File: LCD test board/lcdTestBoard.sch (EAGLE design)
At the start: 1 part

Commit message: Update lcdTestBoard.sch
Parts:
- added C1, C4: 7p, rcl:C-EUC0603
- added C2, C5: 2,2u, rcl:C-EUC0603
- added C3, C6: (no value), rcl:C-EUC0603
- added R1, R4: 1k, rcl:R-EU_R0603
- added R2, R5: (no value), rcl:R-EU_R0603
- added R3, R6: 51,1k, rcl:R-EU_R0603
- added SV1, SV2: (no value), con-lstb:MA04-2
- added SV3: (no value), con-lstb:MA03-1
- added U$1, U$6: LP2980-ADJ, LP2980:LP2980-ADJ
- added U$3: MCP1662, MCP1662:MCP1662
- added U$4: TPS62260, TPS6226x:TPS62260
- added U$5: ST2378E_TSSOP, ST2378E:ST2378E_TSSOP
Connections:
- new net 1.8: SV1.6, SV1.8
- new net 1.8V_LDO: C1.2, C2.1, R2.1, U$1.VOUT
- new net 1.8_LDO: SV1.7
- new net 1.8_STEP: SV1.5
- new net 2.8: SV1.2, SV1.4
- new net 2.8V_LDO: C4.2, C5.1, R5.1, U$6.VOUT
- new net 2.8_LDO: SV1.3
- new net 2.8_STEP: SV1.1
- new net 3V_R: CON1_P2.3V@5, CON1_P2.3V@6, SV2.7
- new net 5V_R: CON1_P2.5V@3, CON1_P2.5V@4, SV2.5
- new net GND: C2.2, C3.1, C5.2, C6.1, CON1_P1.GND@1, CON1_P1.GND@2, CON1_P1.GND@23, CON1_P1.GND@49, CON1_P1.GND@5, CON1_P1.GND@50, CON1_P2.GND@1, CON1_P2.GND@2, CON1_P2.GND@49, CON1_P2.GND@50, R3.1, R6.1, SV2.1, SV3.3, U$1.GND, U$6.GND
- new net N$1: R1.1, U$1.ON/OFF(N)
- new net N$3: C1.1, R2.2, R3.2, U$1.ADJ
- new net N$6: R4.1, U$6.ON/OFF(N)
- new net N$7: SV2.3, SV3.1
- new net N$8: C4.1, R5.2, R6.2, U$6.ADJ
- new net V: C3.2, C6.2, R1.2, R4.2, SV2.2, SV2.4, SV2.6, SV2.8, U$1.VIN, U$6.VIN
- new net VDD: CON1_P1.VDD@3, CON1_P1.VDD@4
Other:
- note added: "1.8V LDO"
- note added: "1.8V LDO 1.8V STEP DOWN 2.8V LDO 2.8V STEP DOWN"
- note added: "2.8V LDO"
- note added: "DISC 3V DISC 5V OUT 3V OUT 5V"
- note added: "Volteage soure select"
- note added: "Voltyge main selector"
- moved on the sheet: CON1_P1, CON1_P2

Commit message: Update lcdTestBoard.sch
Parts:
- added C10, C7: 4.7u, rcl:C-EUC0603
- added C11, C8: 22p, rcl:C-EUC0603
- added C12, C13, C14, C9: 10u, rcl:C-EUC0603
- added D1: BAS40, diode:BAS40
- added L1, L2, L3: 2.2u, rcl:L-USL2012C
- added R10, R7: 180k, rcl:R-EU_R0603
- added R11: 10R, rcl:R-EU_R0603
- added R8: 360k, rcl:R-EU_R0603
- added R9: 680k, rcl:R-EU_R0603
- added SV4: (no value), con-lstb:MA03-1
- added U$2: ST2378E_TSSOP, ST2378E:ST2378E_TSSOP
- added U$7: TPS62260, TPS6226x:TPS62260
- C3, C6: value (none) -> 1u
- R2: value (none) -> 23.7k
- R5: value (none) -> 64.9k
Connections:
- removed net VDD: CON1_P1.VDD@3, CON1_P1.VDD@4
- new net N$10: C8.2, R7.2, R8.1, U$4.FB
- new net N$12: SV4.2, U$3.EN
- new net N$13: D1.A, L3.2, U$3.SW
- new net N$2: L2.1, U$7.SW
- new net N$4: C11.2, R10.2, R9.1, U$7.FB
- new net N$5: L1.1, U$4.SW
- new net V_LCD_N: R11.1, U$3.VFB
- new net V_LCD_P: C13.1, D1.C
- net 1.8_STEP: now also C8.1, C9.1, L1.2, R8.2
- net 2.8_STEP: now also C11.1, C12.1, L2.2, R9.2
- net GND: now also C10.2, C12.2, C13.2, C14.2, C7.2, C9.2, R10.1, R11.2, R7.1, U$3.GND, U$4.GND, U$7.GND
- net V: now also C10.1, C14.1, C7.1, L3.1, SV4.1, U$3.VIN, U$4.EN, U$4.VIN, U$7.EN, U$7.VIN
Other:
- note added: "1.8V STEP DOWN"
- note added: "2.8V STEP DOWN"
- note added: "Curent selector resistor"
- note added: "LCD power regulator"
- note added: "always on external on/off"
- moved on the sheet: U$3, U$4, U$5

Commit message: Update lcdTestBoard.sch
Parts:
- added R12, R13: 1k, rcl:R-EU_R0603
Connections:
- net 1.8 renamed 1.8V
- net 2.8 renamed 2.8V
- net N$1 renamed 1.8_LDO_EN
- net N$6 renamed 2.8_LDO_EN
- new net 1.8_STEP_EN: R12.2, U$4.EN
- new net 2.8_STEP_EN: R13.2, U$7.EN
- new net LCD_POWER_EN: SV4.3
- net GND: now also R1.2, R12.1, R13.1, R4.2
- net V: no longer R1.2, R4.2, U$4.EN, U$7.EN
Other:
- note added: "do rozdzielenia"
- moved on the sheet: C3, C6, L3, R11

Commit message: Update lcdTestBoard.sch
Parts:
- removed SV1: (no value), con-lstb:MA04-2
- added C15: 7p, rcl:C-EUC0603
- added C16: 2,2u, rcl:C-EUC0603
- added C17: 1u, rcl:C-EUC0603
- added C18: 4.7u, rcl:C-EUC0603
- added C19: 22p, rcl:C-EUC0603
- added C20: 10u, rcl:C-EUC0603
- added L4: 2.2u, rcl:L-USL2012C
- added R14, R19: 1k, rcl:R-EU_R0603
- added R15: 82k, rcl:R-EU_R0603
- added R16: 51,1k, rcl:R-EU_R0603
- added R17: 820k, rcl:R-EU_R0603
- added R18: 180k, rcl:R-EU_R0603
- added R20: 3,9k, rcl:R-EU_R0603
- added SV5: (no value), con-lstb:MA06-2
- added U$8: LP2980-ADJ, LP2980:LP2980-ADJ
- added U$9: TPS62260, TPS6226x:TPS62260
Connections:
- new net 3.3V: SV5.2, SV5.4
- new net 3.3V_LDO: C15.2, C16.1, R20.2, U$8.VOUT
- new net 3.3_LDO: SV5.3
- new net 3.3_LDO_EN: R14.1, U$8.ON/OFF(N)
- new net 3.3_STEP: C19.1, C20.1, L4.2, R17.2, SV5.1
- new net 3.3_STEP_EN: R19.2, U$9.EN
- new net N$1: C15.1, R15.2, R16.2, U$8.ADJ
- new net N$11: R15.1, R20.1
- new net N$6: L4.1, U$9.SW
- new net N$9: C19.2, R17.1, R18.2, U$9.FB
- net 1.8V: now also SV5.10, SV5.12; no longer SV1.6, SV1.8
- net 1.8_LDO: now also SV5.11; no longer SV1.7
- net 1.8_STEP: now also SV5.9; no longer SV1.5
- net 2.8V: now also SV5.6, SV5.8; no longer SV1.2, SV1.4
- net 2.8_LDO: now also SV5.7; no longer SV1.3
- net 2.8_STEP: now also SV5.5; no longer SV1.1
- net GND: now also C16.2, C17.1, C18.2, C20.2, R14.2, R16.1, R18.1, R19.1, U$8.GND, U$9.GND
- net V: now also C17.2, C18.1, U$8.VIN, U$9.VIN
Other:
- note added: "1.8V LDO 1.8V STEP DOWN 2.8V LDO 2.8V STEP DOWN 3.3V LDO 3.3V STEP DOWN"
- note added: "3.3V LDO"
- note added: "3.3V STEP DOWN"
- note added: "DISC 3V DISC 5V IN 3.3V IN 5V"
- note removed: "1.8V LDO 1.8V STEP DOWN 2.8V LDO 2.8V STEP DOWN"
- note removed: "DISC 3V DISC 5V OUT 3V OUT 5V"
- moved on the sheet: C1, C10, C11, C12, C13, C14, C2, C3, C4, C5, C6, C7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

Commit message: Update lcdTestBoard.sch
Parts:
- removed U$2, U$5: ST2378E_TSSOP, ST2378E:ST2378E_TSSOP
- added CON2: AXE534124, con_AXE534124:AXE534124
- added SV1: (no value), con-lstb:MA04-2
- added U2, U5: ST2378E_TSSOP, ST2378E:ST2378E_TSSOP
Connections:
- new net LCD_BL_PWM: CON2.LCD_BL_PWM
- new net LCD_CS: CON2.CS
- new net LCD_D0: CON2.D0
- new net LCD_D1: CON2.D1
- new net LCD_D10: CON2.D10
- new net LCD_D11: CON2.D11
- new net LCD_D12: CON2.D12
- new net LCD_D13: CON2.D13
- new net LCD_D14: CON2.D14
- new net LCD_D15: CON2.D15
- new net LCD_D2: CON2.D2
- new net LCD_D3: CON2.D3
- new net LCD_D4: CON2.D4
- new net LCD_D5: CON2.D5
- new net LCD_D6: CON2.D6
- new net LCD_D7: CON2.D7
- new net LCD_D8: CON2.D8
- new net LCD_D9: CON2.D9
- new net LCD_RE: CON2.RE
- new net LCD_RES: CON2.RES
- new net LCD_RS: CON2.RS
- new net LCD_TE: CON2.TE
- new net LCD_WE: CON2.WE
- net 1.8V: now also CON2.VO_DIG, SV1.7, SV1.8
- net 2.8V: now also CON2.VO_LCD_2.8, SV1.5, SV1.6
- net 3.3V: now also SV1.3, SV1.4
- net GND: now also CON2.GND, CON2.Z1, CON2.Z2, CON2.Z3, CON2.Z4, SV1.1, SV1.2
- net V_LCD_N: now also CON2.LCD_BL_K
- net V_LCD_P: now also CON2.LCD_BL_A
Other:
- note added: "Discovery conector"
- note added: "Sony Ericsson U5 Vivaz display"
- note added: "Voltage output"
- moved on the sheet: CON1_P1, CON1_P2

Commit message: Update lcdTestBoard.sch
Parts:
- added U$2: PJST19GL50, con_jack_2.5:PJST19GL50
- added U1: LP2980-ADJ, LP2980:LP2980-ADJ
- added U3: MCP1662, MCP1662:MCP1662
- added U4: TPS62260, TPS6226x:TPS62260
- U$1: value LP2980-ADJ -> PJST19GL50; device LP2980:LP2980-ADJ -> con_jack_2.5:PJST19GL50
- U$3: value MCP1662 -> PJST2538GSD; device MCP1662:MCP1662 -> con_jack_2.5:PJST2538GSD
- U$4: value TPS62260 -> PJST2538GSD; device TPS6226x:TPS62260 -> con_jack_2.5:PJST2538GSD
- renumbered U$6 to U6, U$7 to U7, U$8 to U8, U$9 to U9
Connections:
- net 1.8V_LDO: now also U1.VOUT; no longer U$1.VOUT
- net 1.8_LDO_EN: now also U1.ON/OFF(N); no longer U$1.ON/OFF(N)
- net 1.8_STEP_EN: now also U4.EN; no longer U$4.EN
- net GND: now also U1.GND, U3.GND, U4.GND; no longer U$1.GND, U$3.GND, U$4.GND
- net N$10: now also U4.FB; no longer U$4.FB
- net N$12: now also U3.EN; no longer U$3.EN
- net N$13: now also U3.SW; no longer U$3.SW
- net N$3: now also U1.ADJ; no longer U$1.ADJ
- net N$5: now also U4.SW; no longer U$4.SW
- net V: now also U1.VIN, U3.VIN, U4.VIN; no longer U$1.VIN, U$3.VIN, U$4.VIN
- net V_LCD_N: now also U3.VFB; no longer U$3.VFB

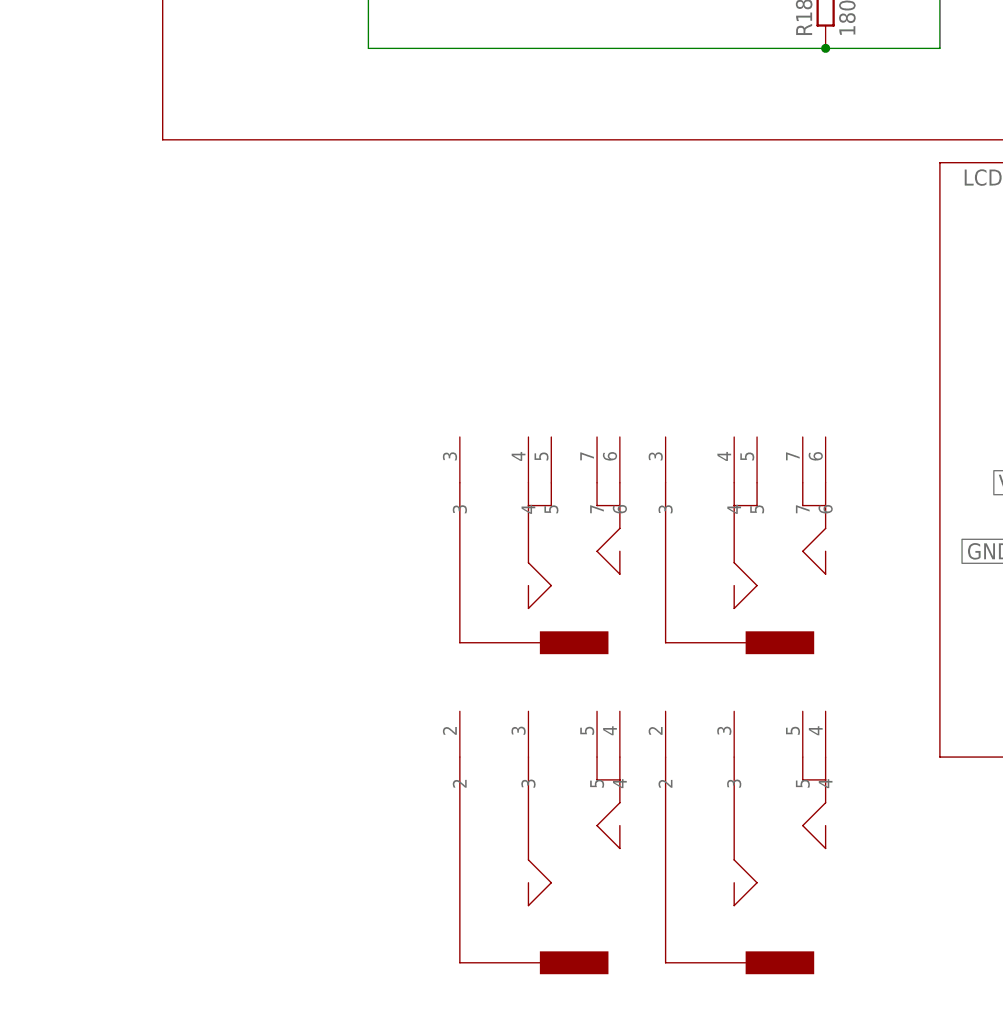
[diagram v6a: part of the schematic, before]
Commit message: dodano zlacza do stackmaty i wyswietlacza
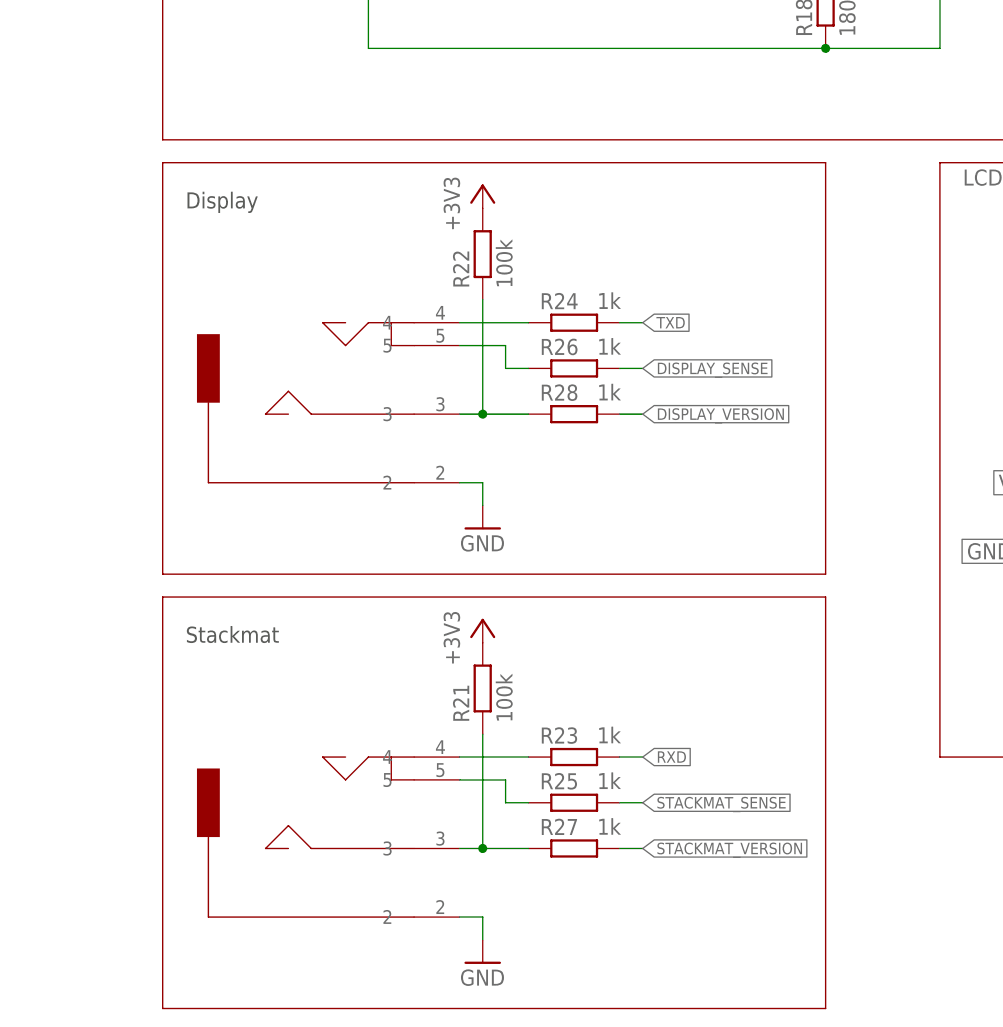
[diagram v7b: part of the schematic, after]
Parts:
- removed U$3, U$4: PJST2538GSD, con_jack_2.5:PJST2538GSD
- added R21, R22: 100k, rcl:R-EU_R0603
- added R23, R24, R25, R26, R27, R28: 1k, rcl:R-EU_R0603
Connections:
- new net +3V3: R21.2, R22.2
- new net DISPLAY_SENSE: R26.1
- new net DISPLAY_VERSION: R28.1
- new net N$14: R22.1, R28.2, U$2.3
- new net N$15: R21.1, R27.2, U$1.3
- new net N$16: R24.2, U$2.4
- new net N$17: R23.2, U$1.4
- new net N$18: R26.2, U$2.5
- new net N$19: R25.2, U$1.5
- new net RXD: R23.1
- new net STACKMAT_SENSE: R25.1
- new net STACKMAT_VERSION: R27.1
- new net TXD: R24.1
- net GND: now also U$1.2, U$2.2
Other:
- note added: "Display"
- note added: "Stackmat"
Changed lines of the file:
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@@
 <part name="U$1" library="con_jack_2.5" deviceset="PJST19GL50" device=""/>
 <part name="U$2" library="con_jack_2.5" deviceset="PJST19GL50" device=""/>
-<part name="U$3" library="con_jack_2.5" deviceset="PJST2538GSD" device=""/>
-<part name="U$4" library="con_jack_2.5" deviceset="PJST2538GSD" device=""/>
+<part name="GND1" library="supply1" deviceset="GND" device=""/>
+<part name="GND2" library="supply1" deviceset="GND" device=""/>
+<part name="R21" library="rcl" deviceset="R-EU_" device="R0603" value="100k"/>
+<part name="R22" library="rcl" deviceset="R-EU_" device="R0603" value="100k"/>
+<part name="R23" library="rcl" deviceset="R-EU_" device="R0603" value="1k"/>
+<part name="R24" library="rcl" deviceset="R-EU_" device="R0603" value="1k"/>
+<part name="R25" library="rcl" deviceset="R-EU_" device="R0603" value="1k"/>
+<part name="R26" library="rcl" deviceset="R-EU_" device="R0603" value="1k"/>
+<part name="R27" library="rcl" deviceset="R-EU_" device="R0603" value="1k"/>
+<part name="R28" library="rcl" deviceset="R-EU_" device="R0603" value="1k"/>
+<part name="+3V1" library="supply1" deviceset="+3V3" device=""/>
+<part name="+3V2" library="supply1" deviceset="+3V3" device=""/>
 </parts>
 <sheets>
@@
 <wire x1="144.78" y1="144.78" x2="144.78" y2="167.64" width="0.1524" layer="94"/>
 <text x="147.32" y="165.1" size="1.778" layer="95">Voltage output</text>
+<text x="190.5" y="96.52" size="1.778" layer="97">Display</text>
+<text x="190.5" y="48.26" size="1.778" layer="97">Stackmat</text>
+<wire x1="261.62" y1="101.6" x2="187.96" y2="101.6" width="0.1524" layer="94"/>
+<wire x1="187.96" y1="101.6" x2="187.96" y2="55.88" width="0.1524" layer="94"/>
+<wire x1="187.96" y1="55.88" x2="261.62" y2="55.88" width="0.1524" layer="94"/>
+<wire x1="261.62" y1="55.88" x2="261.62" y2="101.6" width="0.1524" layer="94"/>
+<wire x1="261.62" y1="53.34" x2="187.96" y2="53.34" width="0.1524" layer="94"/>
+<wire x1="187.96" y1="53.34" x2="187.96" y2="7.62" width="0.1524" layer="94"/>
+<wire x1="187.96" y1="7.62" x2="261.62" y2="7.62" width="0.1524" layer="94"/>
+<wire x1="261.62" y1="7.62" x2="261.62" y2="53.34" width="0.1524" layer="94"/>
 </plain>
 <instances>
@@
 <instance part="CON2" gate="CON$1" x="43.18" y="43.18"/>
 <instance part="SV1" gate="G$1" x="165.1" y="157.48"/>
-<instance part="U$1" gate="G$1" x="254" y="38.1" rot="R270"/>
-<instance part="U$2" gate="G$1" x="231.14" y="38.1" rot="R270"/>
-<instance part="U$3" gate="G$1" x="251.46" y="60.96" rot="R270"/>
-<instance part="U$4" gate="G$1" x="228.6" y="60.96" rot="R270"/>
+<instance part="U$1" gate="G$1" x="218.44" y="27.94" rot="MR0"/>
+<instance part="U$2" gate="G$1" x="218.44" y="76.2" rot="MR0"/>
+<instance part="GND1" gate="1" x="223.52" y="12.7"/>
+<instance part="GND2" gate="1" x="223.52" y="60.96"/>
+<instance part="R21" gate="G$1" x="223.52" y="43.18" rot="R90"/>
+<instance part="R22" gate="G$1" x="223.52" y="91.44" rot="R90"/>
+<instance part="R23" gate="G$1" x="233.68" y="35.56" smashed="yes" rot="R180">
+<attribute name="NAME" x="229.87" y="37.0586" size="1.778" layer="95"/>
+<attribute name="VALUE" x="236.22" y="37.084" size="1.778" layer="96"/>
+</instance>
+<instance part="R24" gate="G$1" x="233.68" y="83.82" smashed="yes" rot="R180">
+<attribute name="NAME" x="229.87" y="85.3186" size="1.778" layer="95"/>
+<attribute name="VALUE" x="236.22" y="85.344" size="1.778" layer="96"/>
+</instance>
+<instance part="R25" gate="G$1" x="233.68" y="30.48" smashed="yes" rot="R180">
+<attribute name="NAME" x="229.87" y="31.9786" size="1.778" layer="95"/>
+<attribute name="VALUE" x="236.22" y="32.004" size="1.778" layer="96"/>
+</instance>
+<instance part="R26" gate="G$1" x="233.68" y="78.74" smashed="yes" rot="R180">
+<attribute name="NAME" x="229.87" y="80.2386" size="1.778" layer="95"/>
+<attribute name="VALUE" x="236.22" y="80.264" size="1.778" layer="96"/>
+</instance>
+<instance part="R27" gate="G$1" x="233.68" y="25.4" smashed="yes" rot="R180">
+<attribute name="NAME" x="229.87" y="26.8986" size="1.778" layer="95"/>
+<attribute name="VALUE" x="236.22" y="26.924" size="1.778" layer="96"/>
+</instance>
+<instance part="R28" gate="G$1" x="233.68" y="73.66" smashed="yes" rot="R180">
+<attribute name="NAME" x="229.87" y="75.1586" size="1.778" layer="95"/>
+<attribute name="VALUE" x="236.22" y="75.184" size="1.778" layer="96"/>
+</instance>
+<instance part="+3V1" gate="G$1" x="223.52" y="99.06"/>
+<instance part="+3V2" gate="G$1" x="223.52" y="50.8"/>
 </instances>
 <busses>
@@
 <wire x1="157.48" y1="152.4" x2="154.94" y2="152.4" width="0.1524" layer="91"/>
 <label x="154.94" y="152.4" size="1.27" layer="95" rot="R180" xref="yes"/>
+</segment>
+<segment>
+<pinref part="U$2" gate="G$1" pin="2"/>
+<pinref part="GND2" gate="1" pin="GND"/>
+<wire x1="220.98" y1="66.04" x2="223.52" y2="66.04" width="0.1524" layer="91"/>
+<wire x1="223.52" y1="66.04" x2="223.52" y2="63.5" width="0.1524" layer="91"/>
+</segment>
+<segment>
+<pinref part="U$1" gate="G$1" pin="2"/>
+<pinref part="GND1" gate="1" pin="GND"/>
+<wire x1="220.98" y1="17.78" x2="223.52" y2="17.78" width="0.1524" layer="91"/>
+<wire x1="223.52" y1="17.78" x2="223.52" y2="15.24" width="0.1524" layer="91"/>
 </segment>
 </net>
@@
 </segment>
 </net>
+<net name="N$14" class="0">
+<segment>
+<pinref part="U$2" gate="G$1" pin="3"/>
+<pinref part="R22" gate="G$1" pin="1"/>
+<wire x1="220.98" y1="73.66" x2="223.52" y2="73.66" width="0.1524" layer="91"/>
+<wire x1="223.52" y1="73.66" x2="223.52" y2="86.36" width="0.1524" layer="91"/>
+<junction x="223.52" y="73.66"/>
+<pinref part="R28" gate="G$1" pin="2"/>
+<wire x1="223.52" y1="73.66" x2="228.6" y2="73.66" width="0.1524" layer="91"/>
+</segment>
+</net>
+<net name="N$15" class="0">
+<segment>
+<pinref part="U$1" gate="G$1" pin="3"/>
+<pinref part="R21" gate="G$1" pin="1"/>
+<wire x1="220.98" y1="25.4" x2="223.52" y2="25.4" width="0.1524" layer="91"/>
+<wire x1="223.52" y1="25.4" x2="223.52" y2="38.1" width="0.1524" layer="91"/>
+<junction x="223.52" y="25.4"/>
+<pinref part="R27" gate="G$1" pin="2"/>
+<wire x1="228.6" y1="25.4" x2="223.52" y2="25.4" width="0.1524" layer="91"/>
+</segment>
+</net>
+<net name="N$16" class="0">
+<segment>
+<pinref part="U$2" gate="G$1" pin="4"/>
+<pinref part="R24" gate="G$1" pin="2"/>
+<wire x1="220.98" y1="83.82" x2="228.6" y2="83.82" width="0.1524" layer="91"/>
+</segment>
+</net>
+<net name="N$17" class="0">
+<segment>
+<pinref part="U$1" gate="G$1" pin="4"/>
+<pinref part="R23" gate="G$1" pin="2"/>
+<wire x1="220.98" y1="35.56" x2="228.6" y2="35.56" width="0.1524" layer="91"/>
+</segment>
+</net>
+<net name="RXD" class="0">
+<segment>
+<pinref part="R23" gate="G$1" pin="1"/>
+<wire x1="238.76" y1="35.56" x2="241.3" y2="35.56" width="0.1524" layer="91"/>
+<label x="241.3" y="35.56" size="1.27" layer="95" xref="yes"/>
+</segment>
+</net>
+<net name="TXD" class="0">
+<segment>
+<pinref part="R24" gate="G$1" pin="1"/>
+<wire x1="238.76" y1="83.82" x2="241.3" y2="83.82" width="0.1524" layer="91"/>
+<label x="241.3" y="83.82" size="1.27" layer="95" xref="yes"/>
+</segment>
+</net>
+<net name="N$19" class="0">
+<segment>
+<pinref part="U$1" gate="G$1" pin="5"/>
+<wire x1="220.98" y1="33.02" x2="226.06" y2="33.02" width="0.1524" layer="91"/>
+<wire x1="226.06" y1="33.02" x2="226.06" y2="30.48" width="0.1524" layer="91"/>
+<pinref part="R25" gate="G$1" pin="2"/>
+<wire x1="226.06" y1="30.48" x2="228.6" y2="30.48" width="0.1524" layer="91"/>
+</segment>
+</net>
+<net name="STACKMAT_SENSE" class="0">
+<segment>
+<pinref part="R25" gate="G$1" pin="1"/>
+<wire x1="238.76" y1="30.48" x2="241.3" y2="30.48" width="0.1524" layer="91"/>
+<label x="241.3" y="30.48" size="1.27" layer="95" xref="yes"/>
+</segment>
+</net>
+<net name="N$18" class="0">
+<segment>
+<pinref part="U$2" gate="G$1" pin="5"/>
+<wire x1="220.98" y1="81.28" x2="226.06" y2="81.28" width="0.1524" layer="91"/>
+<wire x1="226.06" y1="81.28" x2="226.06" y2="78.74" width="0.1524" layer="91"/>
+<pinref part="R26" gate="G$1" pin="2"/>
+<wire x1="226.06" y1="78.74" x2="228.6" y2="78.74" width="0.1524" layer="91"/>
+</segment>
+</net>
+<net name="DISPLAY_SENSE" class="0">
+<segment>
+<pinref part="R26" gate="G$1" pin="1"/>
+<wire x1="238.76" y1="78.74" x2="241.3" y2="78.74" width="0.1524" layer="91"/>
+<label x="241.3" y="78.74" size="1.27" layer="95" xref="yes"/>
+</segment>
+</net>
+<net name="STACKMAT_VERSION" class="0">
+<segment>
+<pinref part="R27" gate="G$1" pin="1"/>
+<wire x1="238.76" y1="25.4" x2="241.3" y2="25.4" width="0.1524" layer="91"/>
+<label x="241.3" y="25.4" size="1.27" layer="95" xref="yes"/>
+</segment>
+</net>
+<net name="DISPLAY_VERSION" class="0">
+<segment>
+<pinref part="R28" gate="G$1" pin="1"/>
+<wire x1="238.76" y1="73.66" x2="241.3" y2="73.66" width="0.1524" layer="91"/>
+<label x="241.3" y="73.66" size="1.27" layer="95" xref="yes"/>
+</segment>
+</net>
+<net name="+3V3" class="0">
+<segment>
+<pinref part="R22" gate="G$1" pin="2"/>
+<pinref part="+3V1" gate="G$1" pin="+3V3"/>
+</segment>
+<segment>
+<pinref part="R21" gate="G$1" pin="2"/>
+<pinref part="+3V2" gate="G$1" pin="+3V3"/>
+</segment>
+</net>
